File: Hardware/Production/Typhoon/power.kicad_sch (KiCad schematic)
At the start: 22 parts, among them J9 Conn_01x01_Socket, U3 LM66200DRLR, U4 MAX77827AEFD+T, U5 SC4215ASTRT, U7 XL1509-3.3

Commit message: Finished footprinting and started the PCB layout
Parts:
- J9: footprint (none) -> Connector_PinSocket_2.54mm:PinSocket_1x01_P2.54mm_Vertical
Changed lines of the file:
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@@
 			)
 		)
-		(property "Footprint" ""
+		(property "Footprint" "Connector_PinSocket_2.54mm:PinSocket_1x01_P2.54mm_Vertical"
 			(at 55.88 82.55 0)
 			(effects

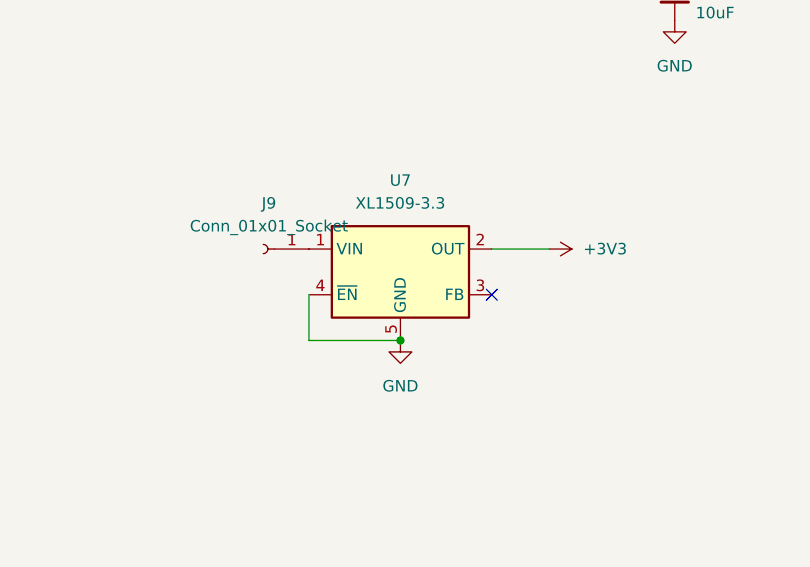
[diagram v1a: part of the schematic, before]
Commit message: Updated schematic, added mosfets to ENN and SPREAD pins of TMC2209 and connected INDEX, CLK, and VREF to GPIO pins
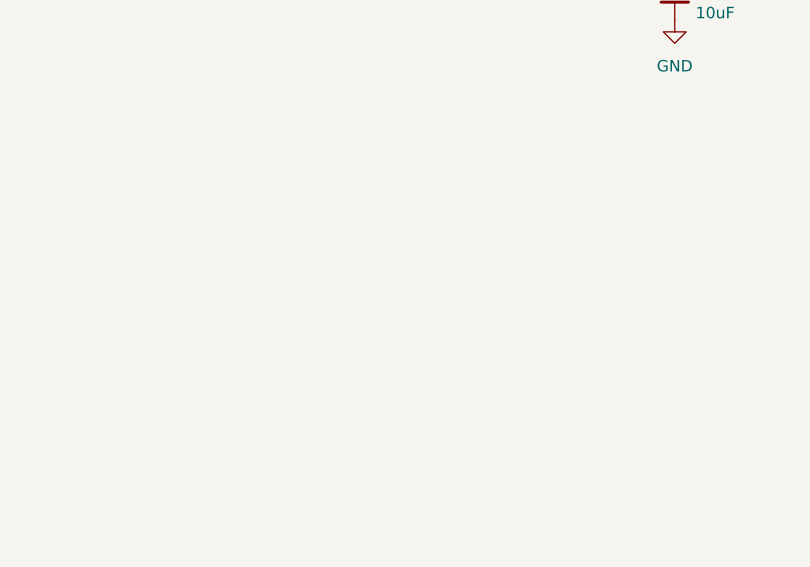
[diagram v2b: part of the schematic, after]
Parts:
- removed J9: Conn_01x01_Socket, Connector_PinSocket_2.54mm:PinSocket_1x01_P2.54mm_Vertical, symbol Connector:Conn_01x01_Socket
- removed U7: XL1509-3.3, Package_SO:SOIC-8_3.9x4.9mm_P1.27mm, symbol Regulator_Switching:XL1509-3.3
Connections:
- no-connect marks 5 -> 4
